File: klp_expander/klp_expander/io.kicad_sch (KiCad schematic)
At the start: 2 parts, among them J1 Conn_02x02_Odd_Even, J2 Conn_02x02_Odd_Even

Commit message: update schematics
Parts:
- added C38, C39, C42, C44, C45: 100n, Capacitor_SMD:C_0402_1005Metric, symbol Device:C
- added C43: 1u, Capacitor_SMD:C_0402_1005Metric, symbol Device:C_Small
- added D10, D8, D9: 1N5819WS, Diode_SMD:D_SOD-323, symbol Diode:1N5819WS
- added D6, D7: BAV99, Package_TO_SOT_SMD:SOT-23, symbol Diode:BAV99
- added J10, J9: USB_A, Connector_USB:USB_A_Connfly_DS1095, symbol Connector:USB_A
- added J11: USB_C_Receptacle_USB2.0_16P, Connector_USB:USB_C_Receptacle_XKB_U262-16XN-4BVC11, symbol Connector:USB_C_Receptacle_USB2.0_16P
- added J3, J4, J5, J6, J7: JST XH 2P, Connector_JST:JST_XH_B2B-XH-A_1x02_P2.50mm_Vertical, symbol Connector_Generic:Conn_01x02
- added J8: JST XH 3P, Connector_JST:JST_XH_B3B-XH-A_1x03_P2.50mm_Vertical, symbol Connector_Generic:Conn_01x03
- added Q1, Q2, Q3: AO3400A, Package_TO_SOT_SMD:SOT-23, symbol Transistor_FET:AO3400A
- added Q4, Q5: AO3401A, Package_TO_SOT_SMD:SOT-23, symbol Transistor_FET:AO3401A
- added R24, R27: 4.7k, Resistor_SMD:R_0402_1005Metric, symbol Device:R
- added R25, R26, R28, R29: 2.37k, Resistor_SMD:R_0402_1005Metric, symbol Device:R
- added R30, R32, R34: 20k, Resistor_SMD:R_0603_1608Metric, symbol Device:R
- added R31, R33, R35: 20, Resistor_SMD:R_0603_1608Metric, symbol Device:R
- added R36, R37, R38, R39, R40, R41: 10k, Resistor_SMD:R_0402_1005Metric, symbol Device:R
- added R42, R43: 100k, Resistor_SMD:R_0402_1005Metric, symbol Device:R
- added R44, R45: 5.1k, Resistor_SMD:R_0402_1005Metric, symbol Device:R_Small
- added U6: 74HCT365D,653, :SOP-16_L10.0-W3.9-P1.27-LS6.0-BL, symbol LCSC:74HCT365D,653
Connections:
- net +24V: now also D10.1 (K), D8.1 (K), D9.1 (K), J5.2 (Pin_2), J6.2 (Pin_2), J7.2 (Pin_2)
- net GND: now also C38.2, C39.2, C42.2, C43.1, C44.1, C45.1, D6.1 (K), D7.1 (K), J10.4 (GND), J11.A1 (GND), J11.A12 (GND), J11.B1 (GND), J11.B12 (GND), J3.1 (Pin_1), J4.1 (Pin_1), J8.1 (Pin_1), J8.3 (Pin_3), J9.4 (GND), Q1.2 (S), Q2.2 (S), Q3.2 (S), R30.1, R32.1, R34.1, R36.2, R37.2, R38.2, R39.2, R40.2, R41.2, R44.2, R45.2, U6.1 (~{OE1}), U6.15 (~{OE2}), U6.8 (GND)
- net IN_DN: now also J11.A7 (D-), J11.B7 (D-)
- net IN_DP: now also J11.A6 (D+), J11.B6 (D+)
- net THR_DN renamed USB_P2_DN
- net THR_DP renamed USB_P2_DP
- new net: D8.2 (A), J5.1 (Pin_1), Q1.3 (D)
- new net: Q2.1 (G), R33.2
- new net: D9.2 (A), J6.1 (Pin_1), Q2.3 (D)
- new net: J4.2 (Pin_2), R27.2, R28.1
- new net: D7.3 (K), R28.2, R29.1
- new net: D6.3 (K), R25.2, R26.1
- new net: J9.1 (VBUS), Q4.3 (D)
- new net: J11.B5 (CC2), R44.1
- new net: D10.2 (A), J7.1 (Pin_1), Q3.3 (D)
- new net: J11.A4 (VBUS), J11.A9 (VBUS), J11.B4 (VBUS), J11.B9 (VBUS)
- new net: J11.A5 (CC1), R45.1
- new net: Q1.1 (G), R31.2
- new net: Q3.1 (G), R35.2
- new net: J10.1 (VBUS), Q5.3 (D)
- new net: J3.2 (Pin_2), R24.2, R25.1
- new net +3.3V: D6.2 (A), D7.2 (A), R24.1, R27.1
- new net +5V: C42.1, C43.2, C44.2, C45.2, Q4.2 (S), Q5.2 (S), R42.2, R43.2, U6.16 (VCC)
- new net FAN_1: R30.2, R31.1, U6.3 (1Y)
- new net FAN_2: R32.2, R33.1, U6.5 (2Y)
- new net FAN_3: R34.2, R35.1, U6.7 (3Y)
- new net GNDS: J10.5 (Shield), J11.S1 (SHIELD), J9.5 (Shield)
- new net GPIO_22: R38.1, U6.6 (3A)
- new net GPIO_23: R37.1, U6.4 (2A)
- new net GPIO_24: R36.1, U6.2 (1A)
- new net GPIO_25: R41.1, U6.14 (6A)
- new net GPIO_26: C38.1, R26.2
- new net GPIO_27: C39.1, R29.2
- new net RGB: J8.2 (Pin_2), U6.13 (6Y)
- new net USB_P3_DN: J10.2 (D-)
- new net USB_P3_DP: J10.3 (D+)
- new net USB_P3_PWR: Q5.1 (G), R43.1
- new net USB_P4_DN: J9.2 (D-)
- new net USB_P4_DP: J9.3 (D+)
- new net USB_P4_PWR: Q4.1 (G), R42.1
- no-connect marks 0 -> 3
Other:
- note added: "Fans"
- note added: "Thermistors"
- note added: "USB In"
- note added: "USB Out"
- moved on the sheet: J2

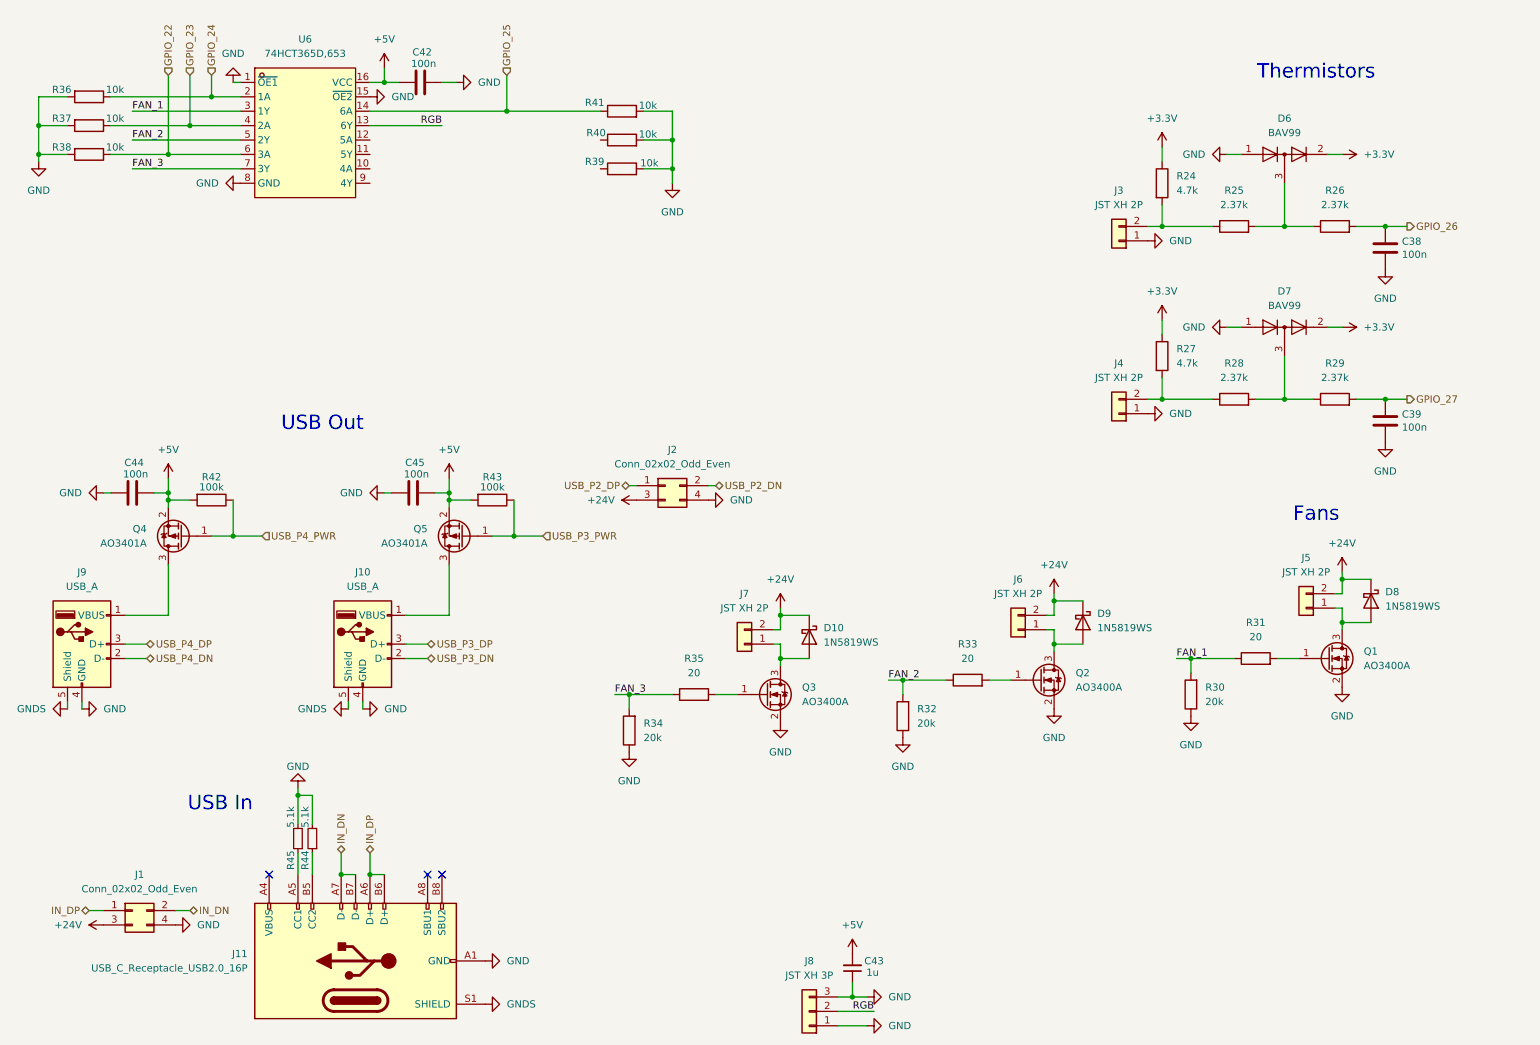
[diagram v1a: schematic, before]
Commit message: feat: merge middle mcu into klp expander. both projects will be merged and will get a new name
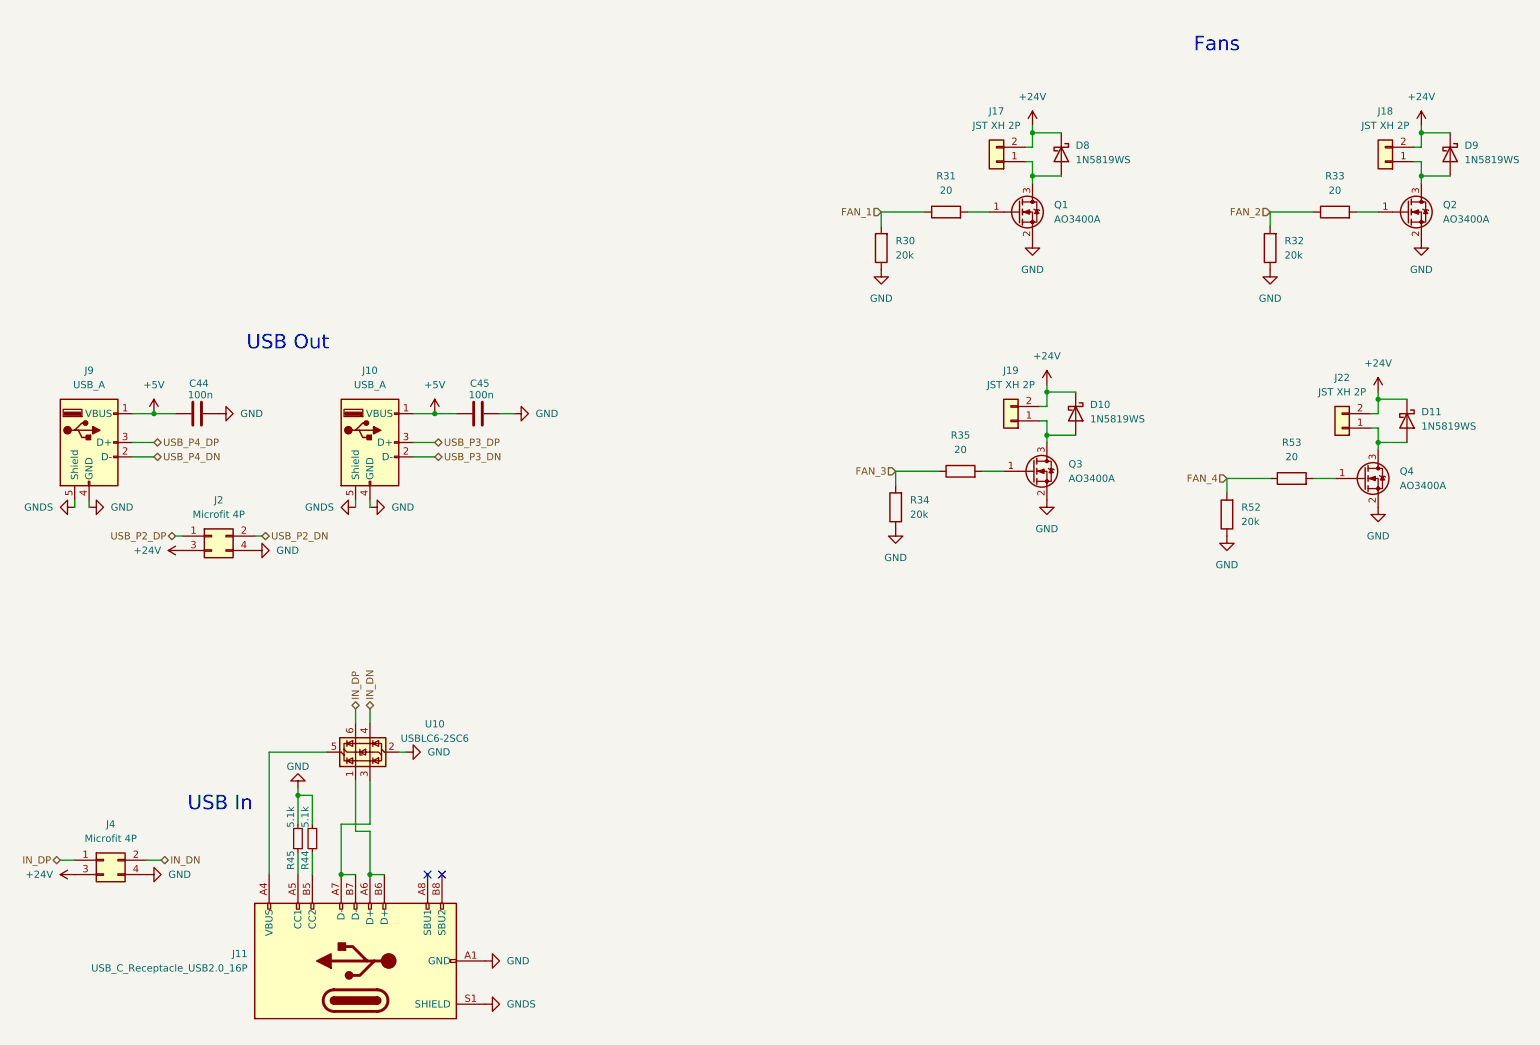
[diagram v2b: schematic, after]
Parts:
- removed C38, C39, C42: 100n, Capacitor_SMD:C_0402_1005Metric, symbol Device:C
- removed C43: 1u, Capacitor_SMD:C_0402_1005Metric, symbol Device:C_Small
- removed D6, D7: BAV99, Package_TO_SOT_SMD:SOT-23, symbol Diode:BAV99
- removed J1: Conn_02x02_Odd_Even, Connector_Molex:Molex_Micro-Fit_3.0_43045-0412_2x02_P3.00mm_Vertical, symbol Connector_Generic:Conn_02x02_Odd_Even
- removed J3, J4, J5, J6, J7: JST XH 2P, Connector_JST:JST_XH_B2B-XH-A_1x02_P2.50mm_Vertical, symbol Connector_Generic:Conn_01x02
- removed J8: JST XH 3P, Connector_JST:JST_XH_B3B-XH-A_1x03_P2.50mm_Vertical, symbol Connector_Generic:Conn_01x03
- removed Q4, Q5: AO3401A, Package_TO_SOT_SMD:SOT-23, symbol Transistor_FET:AO3401A
- removed R24, R27: 4.7k, Resistor_SMD:R_0402_1005Metric, symbol Device:R
- removed R25, R26, R28, R29: 2.37k, Resistor_SMD:R_0402_1005Metric, symbol Device:R
- removed R36, R37, R38, R39, R40, R41: 10k, Resistor_SMD:R_0402_1005Metric, symbol Device:R
- removed R42, R43: 100k, Resistor_SMD:R_0402_1005Metric, symbol Device:R
- removed U6: 74HCT365D,653, :SOP-16_L10.0-W3.9-P1.27-LS6.0-BL, symbol LCSC:74HCT365D,653
- added D11: 1N5819WS, Diode_SMD:D_SOD-323, symbol Diode:1N5819WS
- added J17, J18, J19, J22: JST XH 2P, Connector_JST:JST_XH_S2B-XH-A_1x02_P2.50mm_Horizontal, symbol Connector_Generic:Conn_01x02
- added J4: Microfit 4P, Connector_Molex:Molex_Micro-Fit_3.0_43045-0412_2x02_P3.00mm_Vertical, symbol Connector_Generic:Conn_02x02_Odd_Even
- added Q4: AO3400A, Package_TO_SOT_SMD:SOT-23, symbol Transistor_FET:AO3400A
- added R52: 20k, Resistor_SMD:R_0603_1608Metric, symbol Device:R
- added R53: 20, Resistor_SMD:R_0603_1608Metric, symbol Device:R
- added U10: USBLC6-2SC6, Package_TO_SOT_SMD:SOT-23-6, symbol Power_Protection:USBLC6-2SC6
- J2: value Conn_02x02_Odd_Even -> Microfit 4P
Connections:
- net +24V: now also D11.1 (K), J17.2 (Pin_2), J18.2 (Pin_2), J19.2 (Pin_2), J22.2 (Pin_2), J4.3 (Pin_3)
- net +5V: now also C44.1, C45.1, J10.1 (VBUS), J9.1 (VBUS); no longer C44.2, C45.2
- net GND: now also C44.2, C45.2, J4.4 (Pin_4), Q4.2 (S), R52.1, U10.2 (GND); no longer C44.1, C45.1
- net IN_DN: now also J4.2 (Pin_2), U10.4 (I/O2); no longer J11.A7 (D-), J11.B7 (D-)
- net IN_DP: now also J4.1 (Pin_1), U10.6 (I/O1); no longer J11.A6 (D+), J11.B6 (D+)
- net at D8.2 (A), Q1.3 (D): now also J17.1 (Pin_1)
- net at D9.2 (A), Q2.3 (D): now also J18.1 (Pin_1)
- net at D10.2 (A), Q3.3 (D): now also J19.1 (Pin_1)
- net at J11.A4 (VBUS), J11.A9 (VBUS), J11.B4 (VBUS)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: now also U10.5 (VBUS)
- new net: Q4.1 (G), R53.2
- new net: D11.2 (A), J22.1 (Pin_1), Q4.3 (D)
- new net: J11.A6 (D+), J11.B6 (D+), U10.1 (I/O1)
- new net: J11.A7 (D-), J11.B7 (D-), U10.3 (I/O2)
- new net FAN_4: R52.2, R53.1
- no-connect marks 3 -> 2
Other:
- note removed: "Thermistors"
- moved on the sheet: C44, C45, D10, D8, D9, J10, J9, Q1, Q2, Q3, R30, R31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
